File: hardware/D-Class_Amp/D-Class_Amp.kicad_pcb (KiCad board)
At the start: 2 copper layers, 84 parts, among them J102 AudioJack2, Q501 PHP23NQ11T, Q502 PHP23NQ11T, Q503 PHP23NQ11T, Q504 PHP23NQ11T, U101 NCP1117-12_TO252, U102 MCP1799T-5002H_TT, U201 LM324, U301 TL972, U302 LMV393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

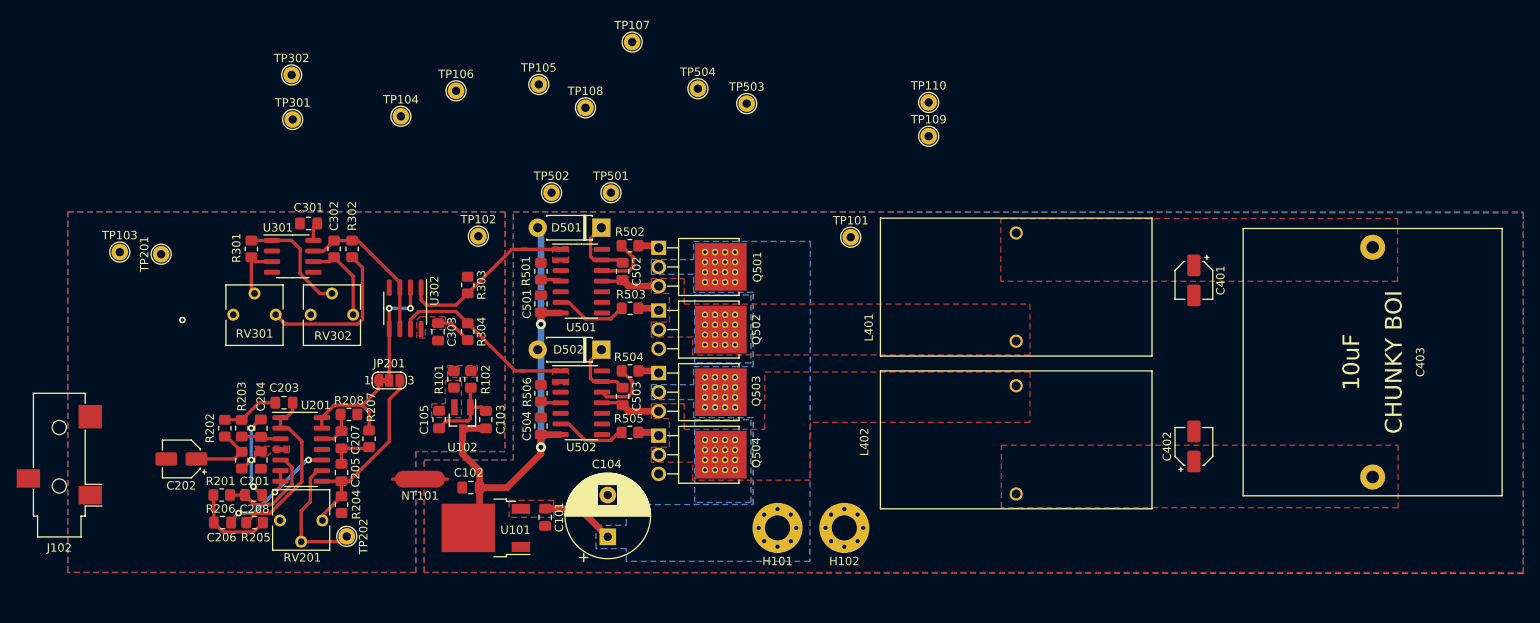
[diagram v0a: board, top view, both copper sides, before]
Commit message: placed and routed all components, fixed the MOSFET footprints, and added all 3D models.
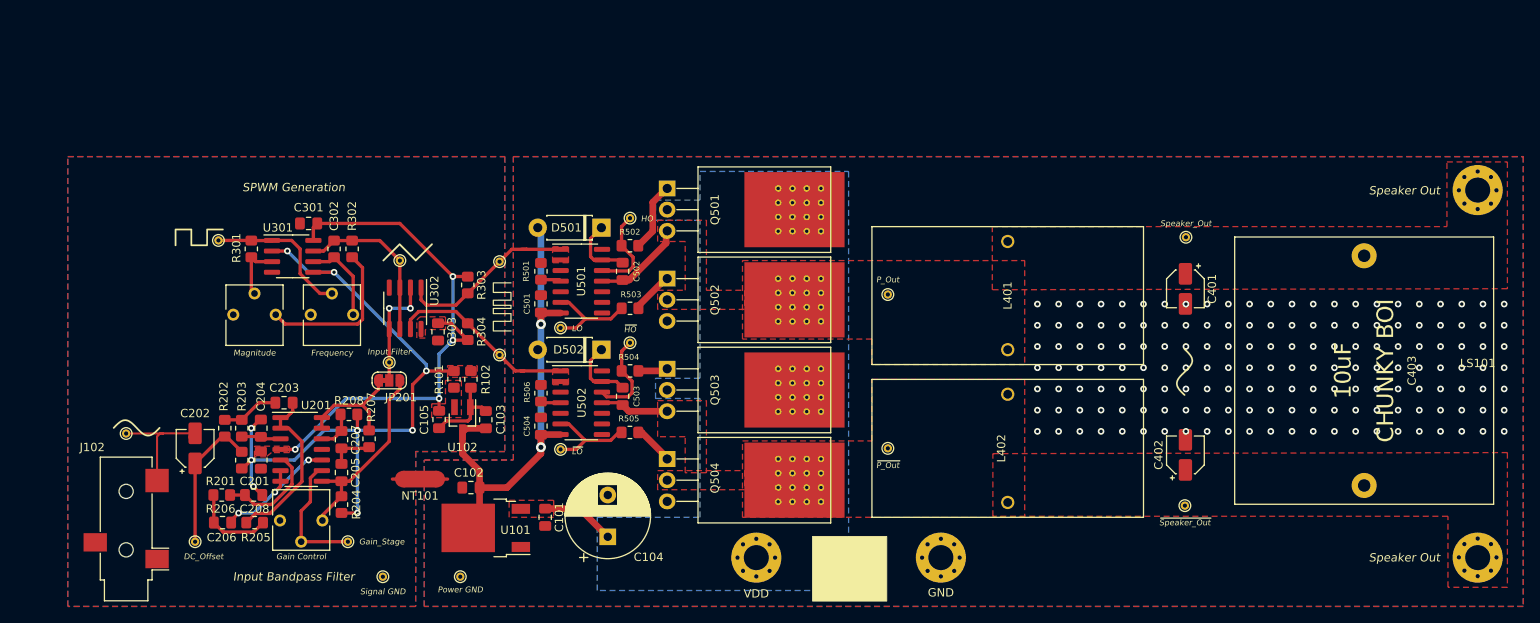
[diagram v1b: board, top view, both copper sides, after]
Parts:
- added G***: LOGO, silk_art:sine, F.Cu at (147.2, 85.2)
- added G***: LOGO, silk_art:SPWM, F.Cu at (65.5, 77.5)
- added G***: LOGO, silk_art:square, F.Cu at (29.1, 69.2)
- added G***: LOGO, silk_art:triangle, F.Cu at (54.1, 71.0)
- added G***: LOGO, silk_art:sine, F.Cu at (21.7, 91.9)
- added LS101: Speaker, Speaker:Speaker, F.Cu at (182.2, 85.4)
- TP101, TP102, TP103, TP104, TP105, TP106, TP107, TP108, TP109, TP110, TP201, TP202, TP301, TP302, TP501, TP502, TP503, TP504: footprint TestPoint:TestPoint_THTPad_D2.0mm_Drill1.0mm -> TestPoint:TestPoint_THTPad_D1.0mm_Drill0.5mm
- moved TP101 61.9 mm to (60.5, 109.7)
- moved TP110 57.2 mm to (147.2, 101.2)
- moved TP108 54.5 mm to (111.6, 94.4)
- moved TP504 46.2 mm to (72.5, 94.5)
- moved TP107 43.0 mm to (111.6, 75.9)
- moved TP102 42.3 mm to (51.2, 109.7)
- moved TP201 34.7 mm to (28.7, 105.5), turned to 0 degrees
- moved TP109 33.1 mm to (147.3, 69.1)
- moved TP106 32.0 mm to (65.2, 83.2)
- moved TP503 31.9 mm to (80.8, 81.7)
- moved TP104 29.5 mm to (51.9, 84.1)
- moved TP302 25.7 mm to (53.2, 71.9)
- moved TP103 21.7 mm to (20.4, 92.6)
- moved TP105 21.7 mm to (65.2, 72.0)
- moved TP301 17.0 mm to (31.5, 69.5)
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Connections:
- RV201 pad 1: Net-(RV201-Pad1) -> (no net)
- RV301 pad 3: Net-(RV301-Pad3) -> (no net)
- RV302 pad 3: Net-(RV302-Pad3) -> (no net)
- U501 pad 10: Net-(U501-Pad10) -> (no net)
- U501 pad 14: Net-(U501-Pad14) -> (no net)
- U501 pad 8: Net-(U501-Pad8) -> (no net)
- U501 pad 9: Net-(U501-Pad9) -> (no net)
- U502 pad 10: Net-(U502-Pad10) -> (no net)
- U502 pad 14: Net-(U502-Pad14) -> (no net)
- U502 pad 8: Net-(U502-Pad8) -> (no net)
- U502 pad 9: Net-(U502-Pad9) -> (no net)
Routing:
- net +2V5: track 11.7 -> 84.7 mm, vias 3 -> 9
- net +5V: track 7.41 -> 68.5 mm, vias 0 -> 4
- net /Input_Stage/SIG_IN: track 0.00 -> 15.1 mm
- net Net-(C202-Pad1): track 8.58 -> 17.1 mm
- net Net-(Q501-Pad1): track 2.55 -> 8.18 mm
- net Net-(R301-Pad1): track 14.0 -> 18.0 mm
- net /Power_Stage/P_OUT: track 7.01 -> 10.8 mm
- net Net-(R504-Pad2): track 7.16 -> 10.9 mm
- net Net-(R502-Pad2): track 7.03 -> 10.8 mm
- net Net-(R503-Pad2): track 8.64 -> 12.1 mm
- net Net-(R505-Pad2): track 8.51 -> 11.9 mm
- net Net-(Q502-Pad1): track 2.53 -> 4.97 mm
- net /S-PWM_Gen/sig_triangle: track 18.5 -> 20.7 mm
- net Net-(Q504-Pad1): track 2.60 -> 4.54 mm
- net Net-(Q503-Pad1): track 2.53 -> 3.48 mm
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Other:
- board text added: "Input Bandpass Filter"
- board text added: "Put the DC jack here bois <3"
- board text added: "SPWM Generation"
- board text added: "Speaker Out"

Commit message: UwU
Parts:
- removed G*** (x2): LOGO, silk_art:sine
- removed G***: LOGO, silk_art:SPWM
- removed G***: LOGO, silk_art:square
- removed G***: LOGO, silk_art:triangle
- added H103: SIG, MountingHole:MountingHole_3mm_Pad_Via, F.Cu at (19.1, 77.5)
- added H104: GNDS, MountingHole:MountingHole_3mm_Pad_Via, F.Cu at (19.1, 64.1)
- added H105: MountingHole_Pad, MountingHole:MountingHole_3.2mm_M3_ISO14580_Pad, F.Cu at (72.5, 60.0)
- added H106: MountingHole_Pad, MountingHole:MountingHole_3.2mm_M3_ISO14580_Pad, F.Cu at (72.5, 115.0)
- added H107: MountingHole_Pad, MountingHole:MountingHole_3.2mm_M3_ISO14580_Pad, F.Cu at (167.5, 60.0)
- added H108: MountingHole_Pad, MountingHole:MountingHole_3.2mm_M3_ISO14580_Pad, F.Cu at (167.5, 115.0)
- added J101: P_IN, Connector_BarrelJack:BarrelJack_Horizontal, F.Cu at (105.2, 105.9)
- J102: footprint Connector_Audio:Jack_3.5mm_CUI_SJ-3523-SMT_Horizontal -> CUI_MJ-63022A:CUI_MJ-63022A
- moved TP103 11.0 mm to (28.7, 85.3)
- moved H101 3.81 mm to (92.1, 107.3)
- moved J102 2.01 mm to (18.8, 102.9), turned to 90 degrees
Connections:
- RV201 pad 1: (no net) -> Net-(RV201-Pad1)
- RV301 pad 3: (no net) -> Net-(RV301-Pad3)
- RV302 pad 3: (no net) -> Net-(RV302-Pad3)
- U501 pad 10: (no net) -> Net-(U501-Pad10)
- U501 pad 14: (no net) -> Net-(U501-Pad14)
- U501 pad 8: (no net) -> Net-(U501-Pad8)
- U501 pad 9: (no net) -> Net-(U501-Pad9)
- U502 pad 10: (no net) -> Net-(U502-Pad10)
- U502 pad 14: (no net) -> Net-(U502-Pad14)
- U502 pad 8: (no net) -> Net-(U502-Pad8)
- U502 pad 9: (no net) -> Net-(U502-Pad9)
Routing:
- net /Input_Stage/SIG_IN: track 15.1 -> 27.1 mm
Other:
- board outline added: 180 x 65 mm
- board text removed: "Put the DC jack here bois <3"

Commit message: PCB done POG
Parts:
- removed H103: SIG, MountingHole:MountingHole_3mm_Pad_Via
- removed H104: GNDS, MountingHole:MountingHole_3mm_Pad_Via
- removed H105, H106, H107, H108: MountingHole_Pad, MountingHole:MountingHole_3.2mm_M3_ISO14580_Pad
- added G***: LOGO, silk_art:thumb, B.Cu at (236.9, 97.9)
- added G***: LOGO, silk_art:triangle, F.Cu at (123.4, 83.4)
- added G***: LOGO, silk_art:sine, F.Cu at (216.7, 97.3)
- added G***: LOGO, silk_art:SPWM, F.Cu at (134.9, 90.2)
- added G***: LOGO, silk_art:square, F.Cu at (98.3, 81.5)
- added G***: LOGO, silk_art:sine, F.Cu at (99.3, 96.8)
- added GNDS: GNDS, MountingHole:MountingHole_3mm_Pad_Via, F.Cu at (88.4, 76.6)
- added M3: MountingHole_Pad, MountingHole:MountingHole_3.2mm_M3_ISO14580_Pad, F.Cu at (236.8, 127.4)
- added M3: MountingHole_Pad, MountingHole:MountingHole_3.2mm_M3_ISO14580_Pad, F.Cu at (236.8, 72.4)
- added M3: MountingHole_Pad, MountingHole:MountingHole_3.2mm_M3_ISO14580_Pad, F.Cu at (141.8, 127.4)
- added M3: MountingHole_Pad, MountingHole:MountingHole_3.2mm_M3_ISO14580_Pad, F.Cu at (141.8, 72.4)
- added SIG: SIG, MountingHole:MountingHole_3mm_Pad_Via, F.Cu at (88.4, 89.9)
- moved H102 72.0 mm to (188.0, 124.2)
- moved H101 72.0 mm to (162.1, 124.1)
- moved C101 70.5 mm to (140.0, 115.1)
- moved C103 70.5 mm to (132.8, 103.4)
- moved C105 70.5 mm to (127.3, 103.4)
- moved C201 70.5 mm to (105.9, 108.2)
- moved C204 70.5 mm to (105.9, 104.4)
- moved C401 70.5 mm to (216.6, 87.7)
- moved C402 70.5 mm to (216.6, 107.6)
- moved J102 70.5 mm to (88.1, 115.3)
- moved NT101 70.5 mm to (125.0, 110.5)
- moved R101 70.5 mm to (129.0, 98.6)
- moved R201 70.5 mm to (103.6, 108.2)
- moved R203 70.5 mm to (103.6, 104.4)
- moved R208 70.5 mm to (116.5, 102.7)
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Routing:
- net GNDS: vias 0 -> 60
- net GND: vias 161 -> 343
- net (no net): vias 0 -> 60
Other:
- board text added: "Contributors --------- Daniel Eisen Nickolai Wolfe Niels Clayton"
- board text added: "Discrete Damplifier"
- board text added: "Rev 1.0"
- board text added: "TM"

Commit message: goddam GNDS bck_plane
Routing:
- net GNDS: vias 60 -> 120
- net (no net): vias 60 -> 0
- added copper zone on B.Cu, net GNDS
- removed copper zone on B.Cu, net (none)

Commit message: res cap to ref
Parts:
- removed G***: LOGO, silk_art:thumb
- removed G***: LOGO, silk_art:triangle
- removed G*** (x2): LOGO, silk_art:sine
- removed G***: LOGO, silk_art:SPWM
- removed G***: LOGO, silk_art:square
- added C106: 100u, Capacitor_SMD:CP_Elec_4x5.4, F.Cu at (98.0, 88.5)
- R303, R304: value 10k -> 1k
- moved TP106 2.21 mm to (133.0, 94.0)
- moved TP105 2.15 mm to (133.0, 86.0)
- renumbered SIG to H103, GNDS to H104, M3 to H105, M3 to H106, M3 to H107, M3 to H108
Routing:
- net +2V5: track 84.7 -> 100.6 mm, vias 9 -> 10

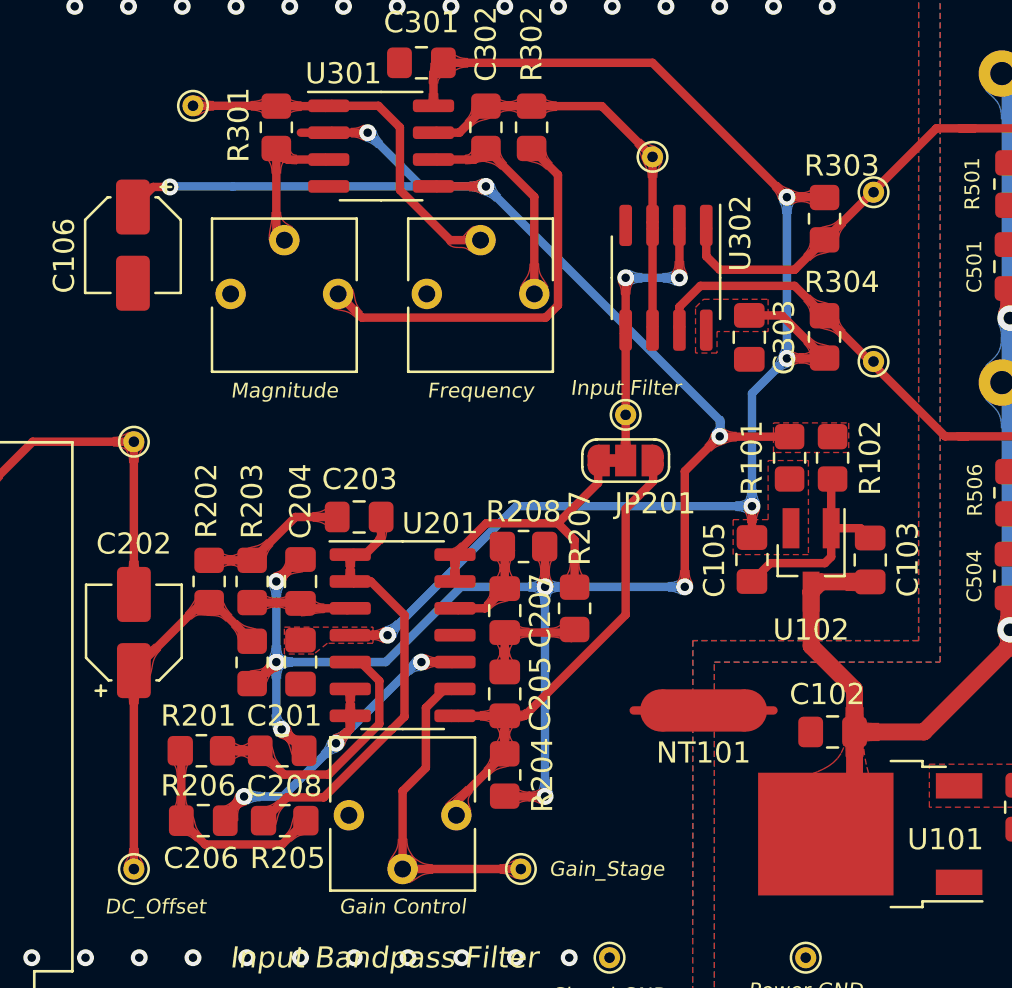
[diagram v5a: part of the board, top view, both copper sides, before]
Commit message: teardrop ref cap, regen BOM
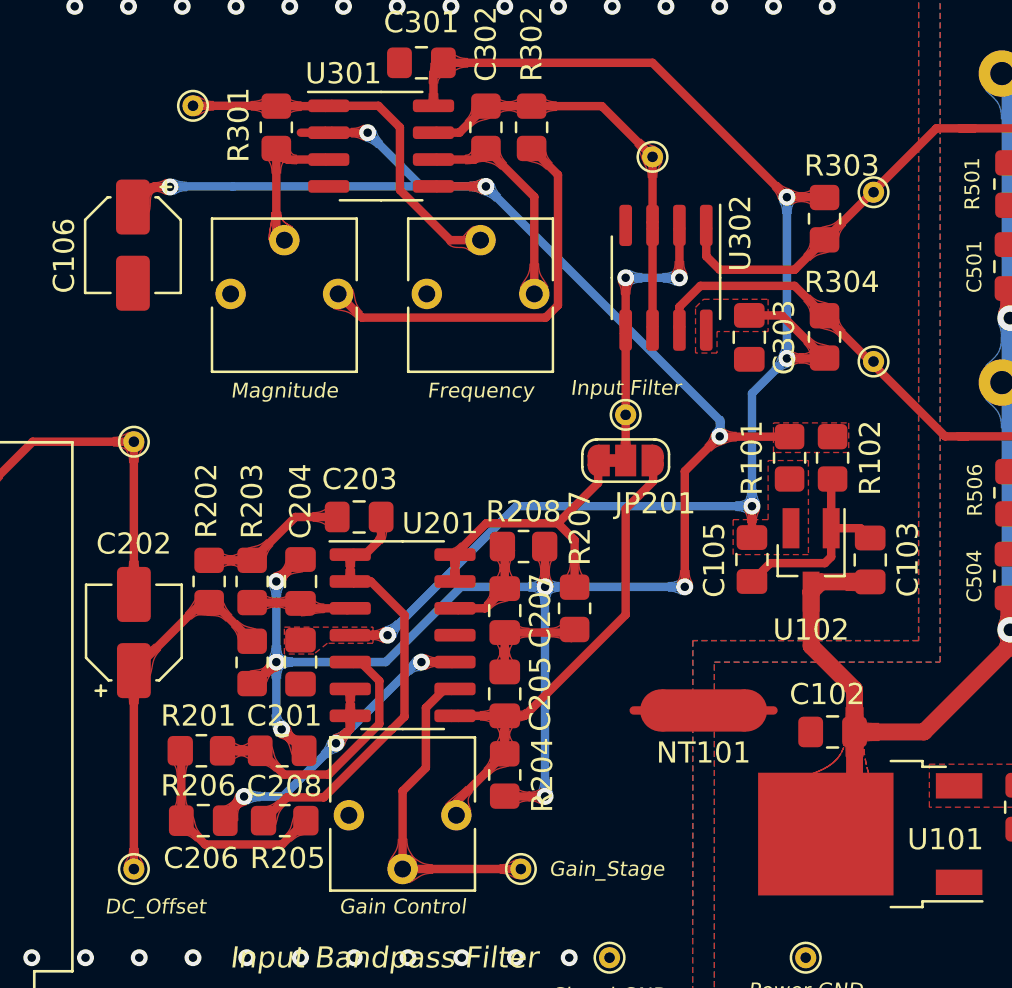
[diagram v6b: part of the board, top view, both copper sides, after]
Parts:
- C106: value 100u -> 100n 16V

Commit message: readded art and regen bom
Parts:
- added G***: LOGO, silk_art:thumb, B.Cu at (240.0, 98.8)
- added G***: LOGO, silk_art:sine, F.Cu at (216.7, 97.1)
- added G***: LOGO, silk_art:SPWM, F.Cu at (135.0, 90.0)
- added G***: LOGO, silk_art:triangle, F.Cu at (123.5, 83.5)
- added G***: LOGO, silk_art:square, F.Cu at (98.5, 81.7)
- added G***: LOGO, silk_art:sine, F.Cu at (99.4, 97.3)
- C106: value 100n 16V -> 100u 6.3V

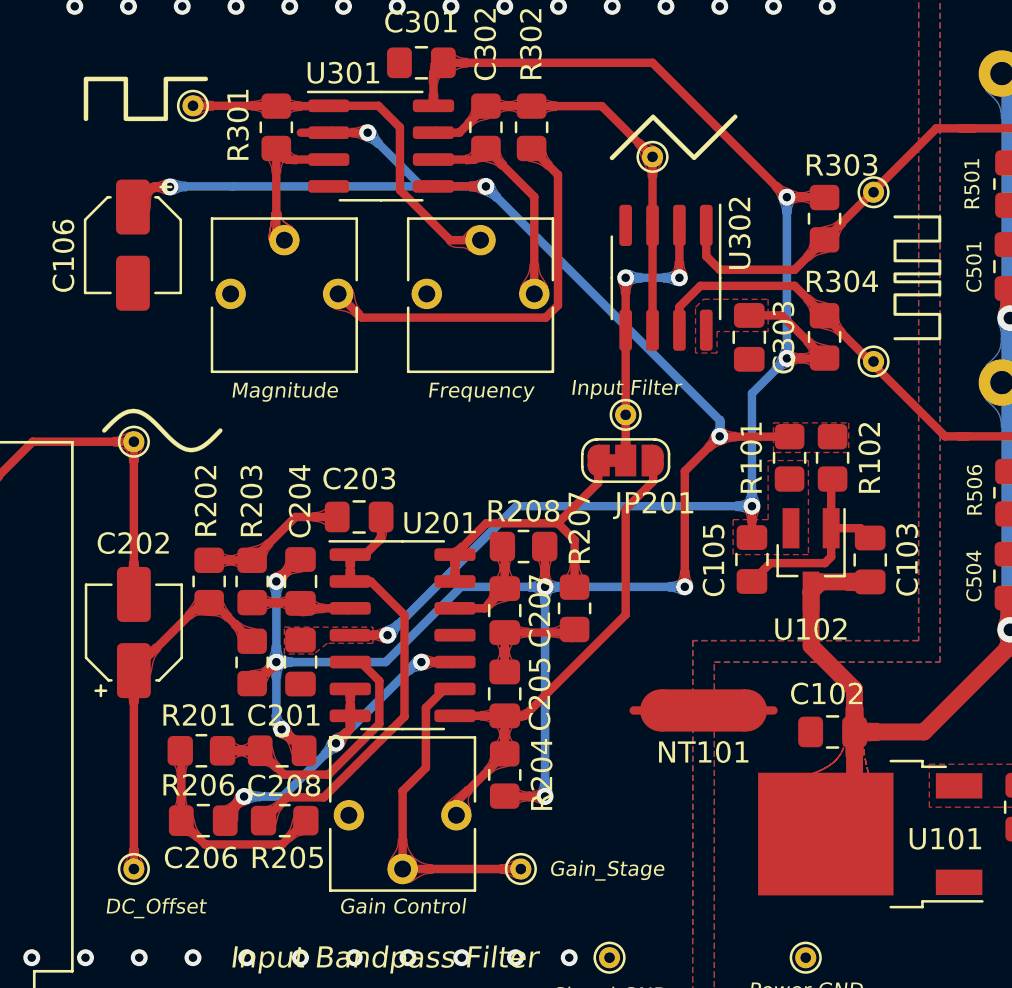
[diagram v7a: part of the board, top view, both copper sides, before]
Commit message: Revert "teardrop ref cap, regen BOM"
This reverts commit 41e1c187b9f88871f416da328e72449a335824d4.
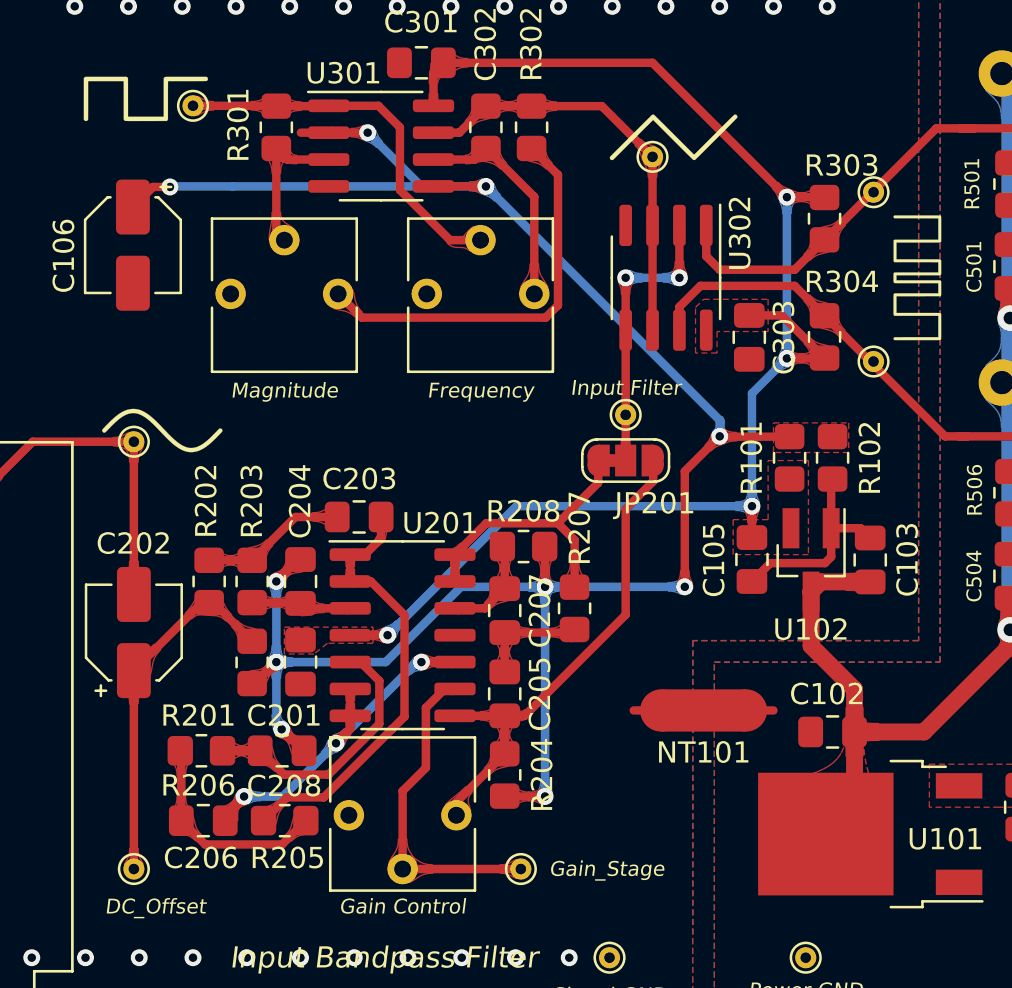
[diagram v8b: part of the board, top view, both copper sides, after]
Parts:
- C106: value 100u 6.3V -> 100u
